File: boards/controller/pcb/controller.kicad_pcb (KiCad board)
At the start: 4 copper layers, 92.4 x 80 mm, 173 parts, among them J14001 Conn_ST_STDC14, J4001 Battery, J5001 DX07S024WJ3R400, Q4001 BSS138, Q6001 BSS138, SW3001 PTS526 SK15 SMTR2 LFS, SW3002 PTS526 SK15 SMTR2 LFS, SW7001 EC11E15204A3, SW8001 EC11E15204A3, SW9001 EC11E15204A3, T2001 150u, U12001 LMR51430YFDDCR, U13001 NJM2884U1-33-TE1, U3001 STM32U575VITx, U4001 3.6, U4002 BQ25792RQMR, U5001 USBLC6-2SC6, U5002 TCPP01-M12, U5003 ISZ065N03L5SATMA1, X3001 16MHz

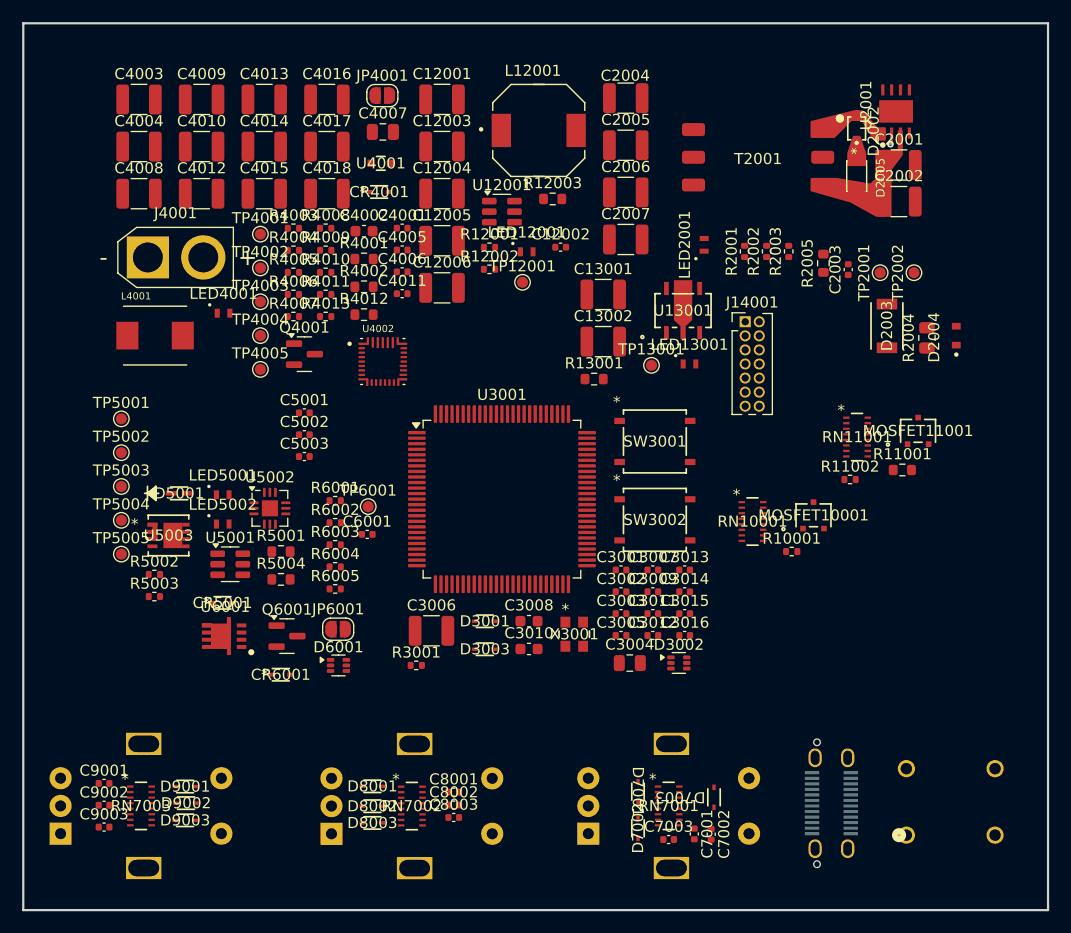
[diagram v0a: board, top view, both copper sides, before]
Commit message: controller: Update BOM
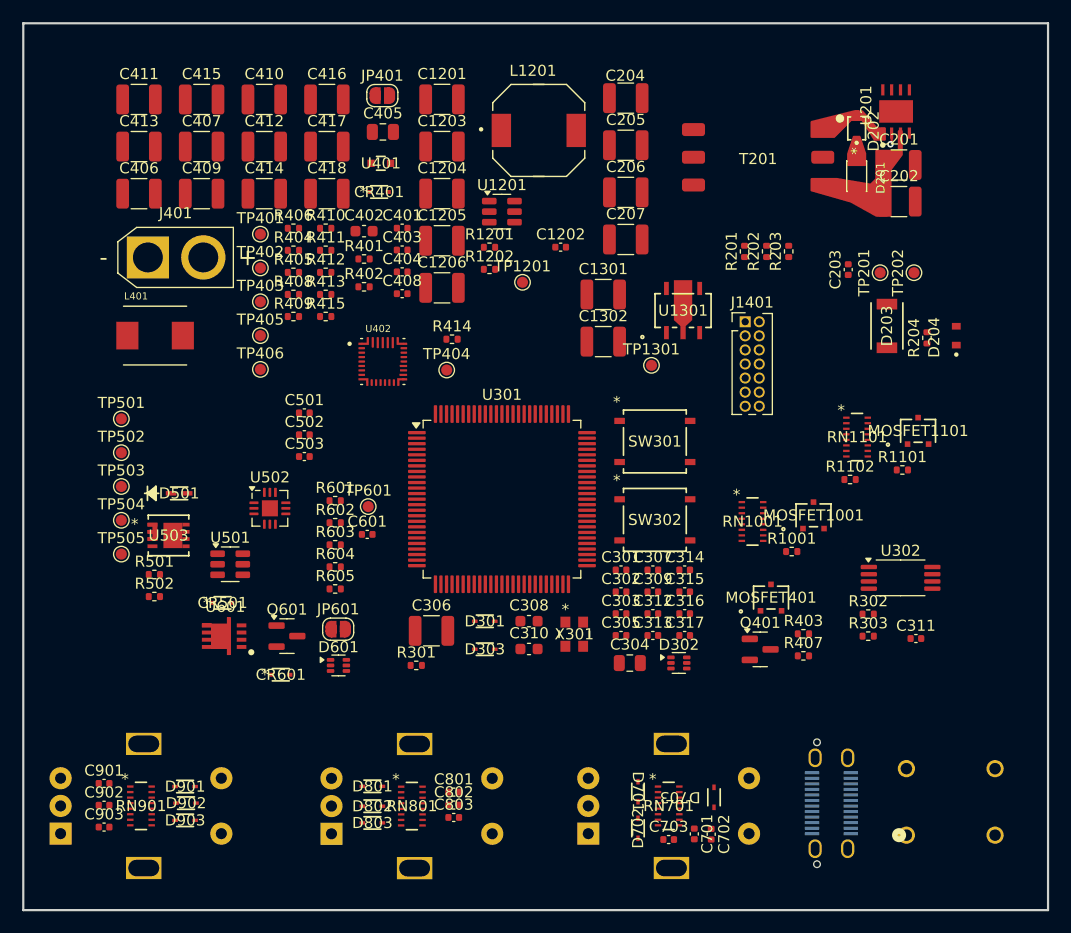
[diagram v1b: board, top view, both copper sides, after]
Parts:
- removed LED12001, LED13001, LED2001, LED4001, LED5001, LED5002: B1911PG--20D000514U1930, B1911PG--20D000514U1930:B1911PG--20D000514U1930
- removed Q4001: BSS138, Package_TO_SOT_SMD:SOT-23
- removed R12003, R4012: 470, Resistor_SMD:R_0603_1608Metric
- removed R13001: 220, Resistor_SMD:R_0603_1608Metric
- removed R2005, R5001, R5004: 2.2k, Resistor_SMD:R_0603_1608Metric
- added C311: 100n, Capacitor_SMD:C_0402_1005Metric, F.Cu at (80.5, 55.5)
- added MOSFET401: SSM3J372R_LF, SSM3J372R_LF:SSM3J372R_LF, F.Cu at (67.5, 51.8)
- added Q401: BSS138, Package_TO_SOT_SMD:SOT-23, F.Cu at (66.5, 56.5)
- added R302: 2.2k, Resistor_SMD:R_0402_1005Metric, F.Cu at (76.2, 53.3)
- added R303: 2.2k, Resistor_SMD:R_0402_1005Metric, F.Cu at (76.2, 55.3)
- added R403: 10k, Resistor_SMD:R_0402_1005Metric, F.Cu at (70.4, 55.1)
- added R407: 10k, Resistor_SMD:R_0402_1005Metric, F.Cu at (70.4, 57.1)
- added R414: 10k, Resistor_SMD:R_0402_1005Metric, F.Cu at (38.7, 28.5)
- added TP404: STAT, TestPoint:TestPoint_Pad_D1.0mm, F.Cu at (38.2, 31.3)
- added U302: CAT24C256, Package_SO:TSSOP-8_4.4x3mm_P0.65mm, F.Cu at (79.1, 50.0)
- D201: renamed from D2005; value BZD27C11PW -> BZD27C27PW
- R1101: renamed from R11001; footprint Resistor_SMD:R_0603_1608Metric -> Resistor_SMD:R_0402_1005Metric
- R204: renamed from R2004; footprint Resistor_SMD:R_0805_2012Metric -> Resistor_SMD:R_0402_1005Metric
- R401: renamed from R4001; footprint Resistor_SMD:R_0603_1608Metric -> Resistor_SMD:R_0402_1005Metric
- R402: renamed from R4002; footprint Resistor_SMD:R_0603_1608Metric -> Resistor_SMD:R_0402_1005Metric
- SW302: renamed from SW3002; value PTS526 SK15 SMTR2 LFS -> PTS526SK15SMTR2 LFS
- renumbered C12001 to C1201, C12002 to C1202, C12003 to C1203, C12004 to C1204, C12005 to C1205, C12006 to C1206, C13001 to C1301, C13002 to C1302, C2001 to C201, C2002 to C202, C2003 to C203, C2004 to C204, C2005 to C205, C2006 to C206, C2007 to C207, C3001 to C301, C3002 to C302, C3003 to C303, C3004 to C304, C3005 to C305, C3006 to C306, C3007 to C307, C3008 to C308, C3009 to C309, C3010 to C310, C3011 to C312, C3012 to C313, C3013 to C314, C3014 to C315, C3015 to C316, C3016 to C317, C4001 to C401, C4002 to C402, C4005 to C403, C4006 to C404, C4007 to C405, C4008 to C406, C4010 to C407, C4011 to C408, C4012 to C409, C4013 to C410, C4003 to C411, C4014 to C412, C4004 to C413, C4015 to C414, C4009 to C415, C4016 to C416, C4017 to C417, C4018 to C418, C5001 to C501, C5002 to C502, C5003 to C503, C6001 to C601, C7001 to C701, C7002 to C702, C7003 to C703, C8001 to C801, C8002 to C802, C8003 to C803, C9001 to C901, C9002 to C902, C9003 to C903, CR4001 to CR401, CR5001 to CR501, CR6001 to CR601, D2002 to D202, D2003 to D203, D2004 to D204, D3001 to D301, D3002 to D302, D3003 to D303, D5001 to D501, D6001 to D601, D7001 to D701, D7002 to D702, D7003 to D703, D8001 to D801, D8002 to D802, D8003 to D803, D9001 to D901, D9002 to D902, D9003 to D903, J14001 to J1401, J4001 to J401, J5001 to J501, JP4001 to JP401, JP6001 to JP601, L12001 to L1201, L4001 to L401, MOSFET10001 to MOSFET1001, MOSFET11001 to MOSFET1101, Q6001 to Q601, R10001 to R1001, R11002 to R1102, R12001 to R1201, R12002 to R1202, R2001 to R201, R2002 to R202, R2003 to R203, R3001 to R301, R4004 to R404, R4005 to R405, R4003 to R406, R4006 to R408, R4007 to R409, R4008 to R410, R4009 to R411, R4010 to R412, R4011 to R413, R4013 to R415, R5002 to R501, R5003 to R502, R6001 to R601, R6002 to R602, R6003 to R603, R6004 to R604, R6005 to R605, RN10001 to RN1001, RN11001 to RN1101, RN7001 to RN701, RN7002 to RN801, RN7003 to RN901, SW3001 to SW301, SW6001 to SW601, SW7001 to SW701, SW8001 to SW801, SW9001 to SW901, T2001 to T201, TP12001 to TP1201, TP13001 to TP1301, TP2001 to TP201, TP2002 to TP202, TP4001 to TP401, TP4002 to TP402, TP4003 to TP403, TP4004 to TP405, TP4005 to TP406, TP5001 to TP501, TP5002 to TP502, TP5003 to TP503, TP5004 to TP504, TP5005 to TP505, TP6001 to TP601, U12001 to U1201, U13001 to U1301, U2001 to U201, U3001 to U301, U4001 to U401, U4002 to U402, U5001 to U501, U5002 to U502, U5003 to U503, U6001 to U601, X3001 to X301
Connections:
- JP401 pad 2: /Charger/VBAT -> Net-(JP401-B)
- R406 pad 1: /Charger/VBAT_SENSE_EN -> /Charger/VBAT
- R406 pad 2: GND -> Net-(MOSFET401-G)
- R408 pad 1: /Charger/VBAT -> Net-(JP401-B)
- R409 pad 2: Net-(Q4001-D) -> GND
- U301 pad 92: unconnected-(U3001-PB6-Pad92) -> /Microcontroller/EEPROM_SCL
- U301 pad 93: unconnected-(U3001-PB7-Pad93) -> /Microcontroller/EEPROM_SDA
- U401 pad 2: Net-(Q4001-D) -> GND
